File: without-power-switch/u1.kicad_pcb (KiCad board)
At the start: 2 copper layers, 18 x 16.5 mm, 10 parts, among them J1 USB_C_Receptacle_USB2.0, J2 Conn_01x06_MountingPin, U1 USBLC6-2P6

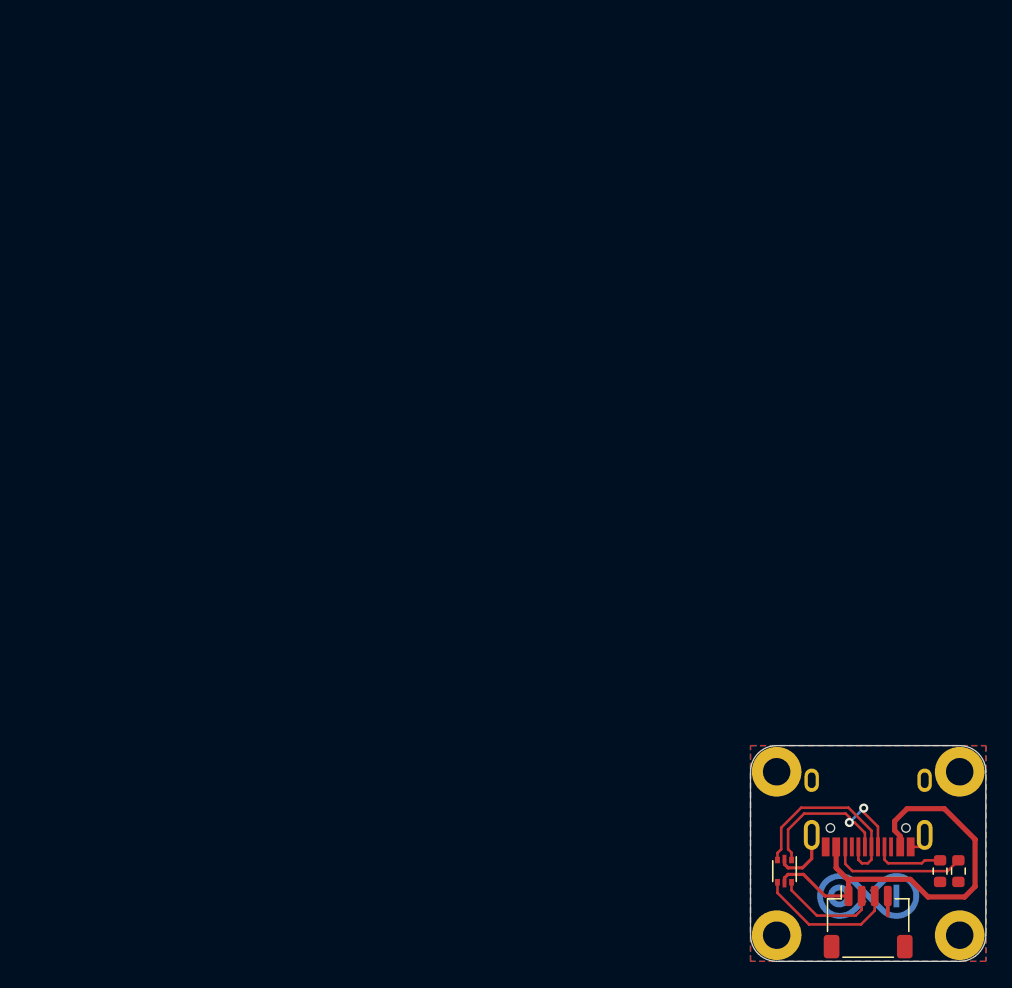
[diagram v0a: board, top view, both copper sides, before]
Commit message: Add warped design
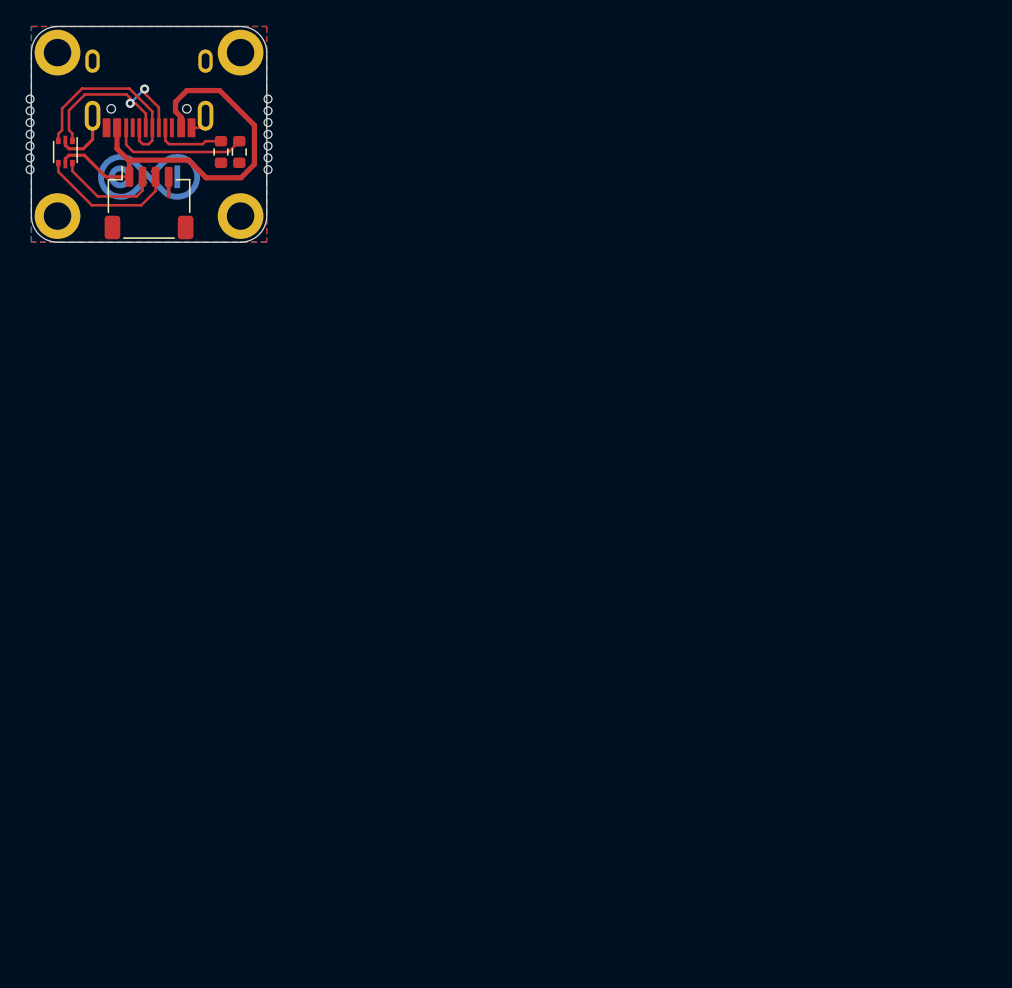
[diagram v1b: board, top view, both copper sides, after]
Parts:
- added REF**: Mouse_Bite_7, u1:Mouse_Bite_7, F.Cu at (45.0, 43.2)
- added REF**: Mouse_Bite_7, u1:Mouse_Bite_7, F.Cu at (63.0, 43.2)
- moved G*** 77.8 mm to (54.0, 46.5)
- moved J1 77.8 mm to (54.0, 38.7)
- moved J2 77.8 mm to (54.0, 48.5)
- moved R2 77.8 mm to (60.9, 44.6)
- moved REF** 77.8 mm to (61.0, 49.5)
- moved REF** 77.8 mm to (47.0, 49.5)
- moved REF** 77.8 mm to (61.0, 37.0)
- moved REF** 77.8 mm to (47.0, 37.0)
- moved R1 77.8 mm to (59.5, 44.6)
- moved U1 77.8 mm to (47.6, 44.6)
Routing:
- net UVCC: track 34.2 -> 33.6 mm
